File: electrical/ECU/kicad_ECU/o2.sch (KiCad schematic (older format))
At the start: 3 parts

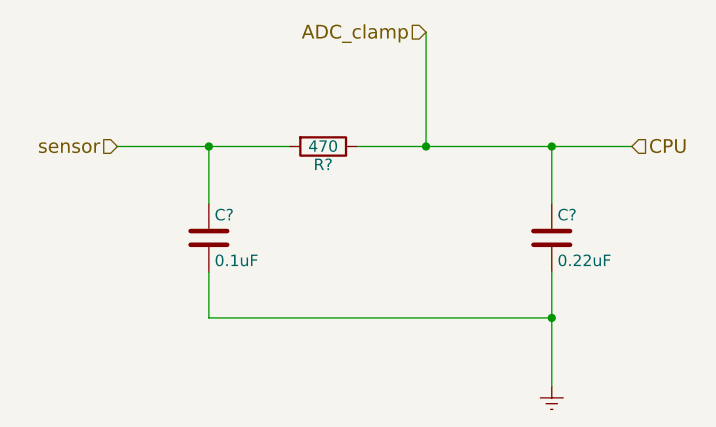
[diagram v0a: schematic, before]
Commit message: fixed some naming errors and initial round of double checking
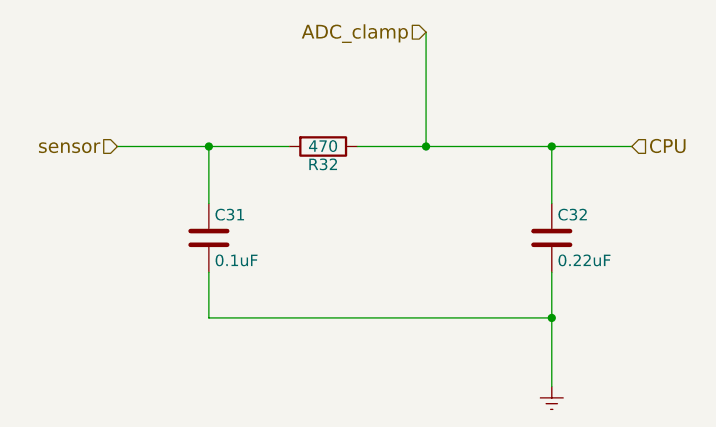
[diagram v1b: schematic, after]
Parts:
- gave numbers to parts that had none: 3
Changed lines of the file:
@@
 $Descr A4 11693 8268
 encoding utf-8
-Sheet 9 33
+Sheet 13 33
 Title "O2 Sensor"
 Date ""
@@
 CPU
 $Comp
-L R R?
+L R R32
 U 1 1 597752E7
 P 5600 3250
-F 0 "R?" V 5680 3250 50  0000 C CNN
+F 0 "R32" V 5680 3250 50  0000 C CNN
 F 1 "470" V 5600 3250 50  0000 C CNN
 F 2 "" V 5530 3250 50  0001 C CNN
@@
 $EndComp
 $Comp
-L C C?
+L C C31
 U 1 1 5977530D
 P 5100 3650
-F 0 "C?" H 5125 3750 50  0000 L CNN
+F 0 "C31" H 5125 3750 50  0000 L CNN
 F 1 "0.1uF" H 5125 3550 50  0000 L CNN
 F 2 "" H 5138 3500 50  0001 C CNN
@@
 $EndComp
 $Comp
-L C C?
+L C C32
 U 1 1 59775333
 P 6600 3650
-F 0 "C?" H 6625 3750 50  0000 L CNN
+F 0 "C32" H 6625 3750 50  0000 L CNN
 F 1 "0.22uF" H 6625 3550 50  0000 L CNN
 F 2 "" H 6638 3500 50  0001 C CNN
@@
 $EndComp
 $Comp
-L Earth #PWR?
+L Earth #PWR40
 U 1 1 59775372
 P 6600 4300
-F 0 "#PWR?" H 6600 4050 50  0001 C CNN
+F 0 "#PWR40" H 6600 4050 50  0001 C CNN
 F 1 "Earth" H 6600 4150 50  0001 C CNN
 F 2 "" H 6600 4300 50  0001 C CNN
